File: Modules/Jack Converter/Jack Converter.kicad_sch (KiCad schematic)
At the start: 0 parts

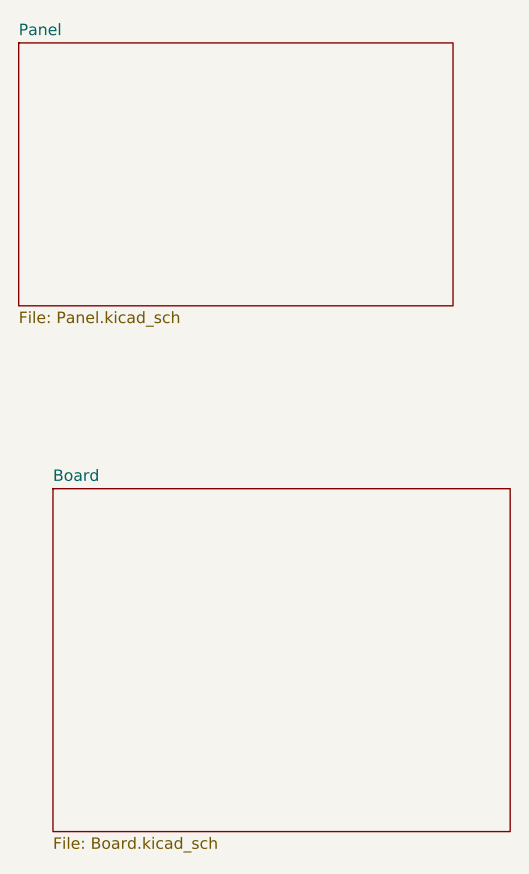
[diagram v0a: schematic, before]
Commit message: Deleted Panel sch sheet
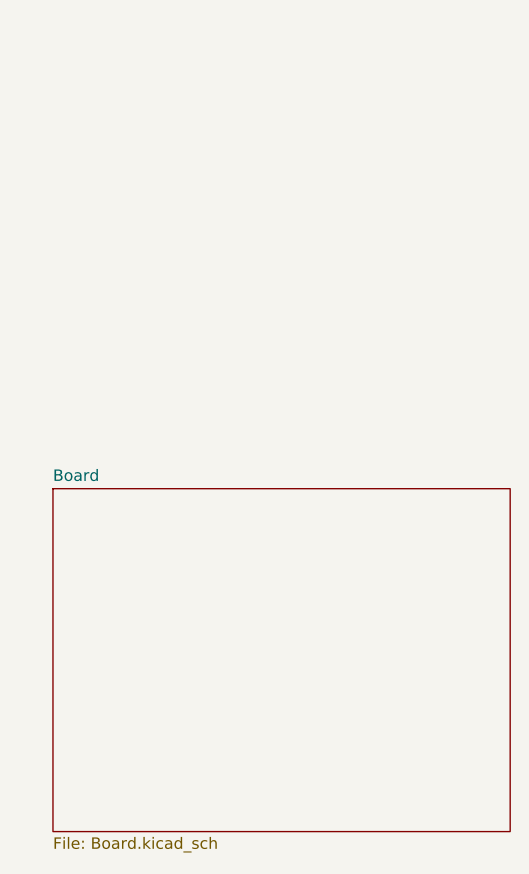
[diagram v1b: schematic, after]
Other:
- removed sheet Panel
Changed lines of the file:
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@@
-		)
-	)
-	(sheet
-		(at 60.96 49.53)
-		(size 48.26 29.21)
-		(fields_autoplaced yes)
-		(stroke
-			(width 0.1524)
-			(type solid)
-		)
-		(fill
-			(color 0 0 0 0.0000)
-		)
-		(property "Sheetname" "Panel"
-			(at 60.96 48.8184 0)
-			(effects
-				(font
-					(size 1.27 1.27)
-				)
-				(justify left bottom)
-			)
-		)
-		(property "Sheetfile" "Panel.kicad_sch"
-			(at 60.96 79.3246 0)
-			(effects
-				(font
-					(size 1.27 1.27)
-				)
-				(justify left top)
-			)
-		)
-		(instances
-			(project "Jack Converter"
-				(path "/b497d75e-0918-4e9c-ae43-36360bc031dc"
-					(page "2")
-				)
-			)
 		)
 	)
